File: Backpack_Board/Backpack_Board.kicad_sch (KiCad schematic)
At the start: 8 parts, among them J1 Conn_01x05, U7 MAX30102EFD_T

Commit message: Completed Backpack Board
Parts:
- removed J1: Conn_01x05, Connector_PinHeader_1.27mm:PinHeader_1x05_P1.27mm_Vertical, symbol Connector_Generic:Conn_01x05
- added J1, J2: Conn_01x03, Connector_PinHeader_1.27mm:PinHeader_1x03_P1.27mm_Vertical, symbol Connector_Generic:Conn_01x03
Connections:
- net +1V8: now also J2.3 (Pin_3)
- net GND: now also J2.1 (Pin_1)
- net MAX_INT: now also J2.2 (Pin_2)
- net SCL: now also J1.1 (Pin_1)
- net SDA: now also J1.2 (Pin_2)
- no-connect marks 1 -> 2
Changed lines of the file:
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@@
+	)
+	(no_connect
+		(at 54.61 101.6)
 	)
 	(no_connect
@@
 	(wire
 		(pts
+			(xy 63.5 82.55) (xy 54.61 82.55)
+		)
+		(stroke
+			(width 0)
+			(type default)
+		)
+	)
+	(wire
+		(pts
 			(xy 96.52 77.47) (xy 96.52 78.74)
 		)
@@
 	(wire
 		(pts
-			(xy 63.5 91.44) (xy 54.61 91.44)
-		)
-		(stroke
-			(width 0)
-			(type default)
-		)
-	)
-	(wire
-		(pts
 			(xy 115.57 119.38) (xy 115.57 120.65)
 		)
@@
 	(wire
 		(pts
+			(xy 54.61 80.01) (xy 63.5 80.01)
+		)
+		(stroke
+			(width 0)
+			(type default)
+		)
+	)
+	(wire
+		(pts
 			(xy 107.95 118.11) (xy 107.95 119.38)
 		)
@@
 	(wire
 		(pts
-			(xy 63.5 101.6) (xy 54.61 101.6)
-		)
-		(stroke
-			(width 0)
-			(type default)
-		)
-	)
-	(wire
-		(pts
 			(xy 139.7 109.22) (xy 139.7 106.68)
 		)
@@
 	(wire
 		(pts
-			(xy 63.5 93.98) (xy 54.61 93.98)
-		)
-		(stroke
-			(width 0)
-			(type default)
-		)
-	)
-	(wire
-		(pts
 			(xy 107.95 129.54) (xy 115.57 129.54)
 		)
@@
 	(wire
 		(pts
+			(xy 54.61 77.47) (xy 63.5 77.47)
+		)
+		(stroke
+			(width 0)
+			(type default)
+		)
+	)
+	(wire
+		(pts
 			(xy 115.57 128.27) (xy 115.57 129.54)
 		)
@@
 		)
 	)
-	(label "MAX_INT"
-		(at 63.5 93.98 180)
+	(label "+1V8"
+		(at 63.5 82.55 180)
 		(effects
 			(font
@@
 		)
 	)
-	(label "+1V8"
-		(at 63.5 91.44 180)
+	(label "GND"
+		(at 63.5 77.47 180)
 		(effects
 			(font
@@
 		)
 	)
-	(label "GND"
-		(at 63.5 101.6 180)
+	(label "MAX_INT"
+		(at 63.5 80.01 180)
 		(effects
 			(font
@@
 			)
 			(justify left bottom)
+		)
+	)
+	(symbol
+		(lib_id "Connector_Generic:Conn_01x03")
+		(at 49.53 80.01 0)
+		(mirror y)
+		(unit 1)
+		(body_style 1)
+		(exclude_from_sim no)
+		(in_bom yes)
+		(on_board yes)
+		(in_pos_files yes)
+		(dnp no)
+		(property "Reference" "J2"
+			(at 49.53 87.9645 0)
+			(show_name no)
+			(do_not_autoplace no)
+			(effects
+				(font
+					(size 1.27 1.27)
+				)
+			)
+		)
+		(property "Value" "Conn_01x03"
+			(at 49.53 85.5402 0)
+			(show_name no)
+			(do_not_autoplace no)
+			(effects
+				(font
+					(size 1.27 1.27)
+				)
+			)
+		)
+		(property "Footprint" "Connector_PinHeader_1.27mm:PinHeader_1x03_P1.27mm_Vertical"
+			(at 49.53 80.01 0)
+			(hide yes)
+			(show_name no)
+			(do_not_autoplace no)
+			(effects
+				(font
+					(size 1.27 1.27)
+				)
+			)
+		)
+		(property "Datasheet" ""
+			(at 49.53 80.01 0)
+			(hide yes)
+			(show_name no)
+			(do_not_autoplace no)
+			(effects
+				(font
+					(size 1.27 1.27)
+				)
+			)
+		)
+		(property "Description" "Generic connector, single row, 01x03, script generated (kicad-library-utils/schlib/autogen/connector/)"
+			(at 49.53 80.01 0)
+			(hide yes)
+			(show_name no)
+			(do_not_autoplace no)
+			(effects
+				(font
+					(size 1.27 1.27)
+				)
+			)
+		)
+		(pin "2"
+		)
+		(pin "1"
+		)
+		(pin "3"
+		)
+		(instances
+			(project "Backpack_Board"
+				(path "/49f0e556-777a-4724-8c92-dc192098b240"
+					(reference "J2")
+					(unit 1)
+				)
+			)
+		)
+	)
+	(symbol
+		(lib_id "Connector_Generic:Conn_01x03")
+		(at 49.53 99.06 0)
+		(mirror y)
+		(unit 1)
+		(body_style 1)
+		(exclude_from_sim no)
+		(in_bom yes)
+		(on_board yes)
+		(in_pos_files yes)
+		(dnp no)
+		(property "Reference" "J1"
+			(at 49.53 107.0145 0)
+			(show_name no)
+			(do_not_autoplace no)
+			(effects
+				(font
+					(size 1.27 1.27)
+				)
+			)
+		)
+		(property "Value" "Conn_01x03"
+			(at 49.53 104.5902 0)
+			(show_name no)
+			(do_not_autoplace no)
+			(effects
+				(font
+					(size 1.27 1.27)
+				)
+			)
+		)
+		(property "Footprint" "Connector_PinHeader_1.27mm:PinHeader_1x03_P1.27mm_Vertical"
+			(at 49.53 99.06 0)
+			(hide yes)
+			(show_name no)
+			(do_not_autoplace no)
+			(effects
+				(font
+					(size 1.27 1.27)
+				)
+			)
+		)
+		(property "Datasheet" ""
+			(at 49.53 99.06 0)
+			(hide yes)
+			(show_name no)
+			(do_not_autoplace no)
+			(effects
+				(font
+					(size 1.27 1.27)
+				)
+			)
+		)
+		(property "Description" "Generic connector, single row, 01x03, script generated (kicad-library-utils/schlib/autogen/connector/)"
+			(at 49.53 99.06 0)
+			(hide yes)
+			(show_name no)
+			(do_not_autoplace no)
+			(effects
+				(font
+					(size 1.27 1.27)
+				)
+			)
+		)
+		(pin "2"
+		)
+		(pin "1"
+		)
+		(pin "3"
+		)
+		(instances
+			(project "Backpack_Board"
+				(path "/49f0e556-777a-4724-8c92-dc192098b240"
+					(reference "J1")
+					(unit 1)
+				)
+			)
 		)
 	)
@@
 				)
 			)
-		)
-	)
-	(symbol
-		(lib_id "Connector_Generic:Conn_01x05")
-		(at 49.53 96.52 180)
-		(unit 1)
-		(body_style 1)
-		(exclude_from_sim no)
-		(in_bom yes)
-		(on_board yes)
-		(in_pos_files yes)
-		(dnp no)
-		(fields_autoplaced yes)
-		(property "Reference" "J1"
-			(at 49.53 86.0255 0)
-			(show_name no)
-			(do_not_autoplace no)
-			(effects
-				(font
-					(size 1.27 1.27)
-				)
-			)
-		)
-		(property "Value" "Conn_01x05"
-			(at 49.53 88.4498 0)
-			(show_name no)
-			(do_not_autoplace no)
-			(effects
-				(font
-					(size 1.27 1.27)
-				)
-			)
-		)
-		(property "Footprint" "Connector_PinHeader_1.27mm:PinHeader_1x05_P1.27mm_Vertical"
-			(at 49.53 96.52 0)
-			(hide yes)
-			(show_name no)
-			(do_not_autoplace no)
-			(effects
-				(font
-					(size 1.27 1.27)
-				)
-			)
-		)
-		(property "Datasheet" ""
-			(at 49.53 96.52 0)
-			(hide yes)
-			(show_name no)
-			(do_not_autoplace no)
-			(effects
-				(font
-					(size 1.27 1.27)
-				)
-			)
-		)
-		(property "Description" "Generic connector, single row, 01x05, script generated (kicad-library-utils/schlib/autogen/connector/)"
-			(at 49.53 96.52 0)
-			(hide yes)
-			(show_name no)
-			(do_not_autoplace no)
-			(effects
-				(font
-					(size 1.27 1.27)
-				)
-			)
-		)
-		(pin "2"
-		)
-		(pin "1"
-		)
-		(pin "3"
-		)
-		(pin "4"
-		)
-		(pin "5"
-		)
-		(instances
-			(project "Backpack_Board"
-				(path "/49f0e556-777a-4724-8c92-dc192098b240"
-					(reference "J1")
-					(unit 1)
-				)
-			)

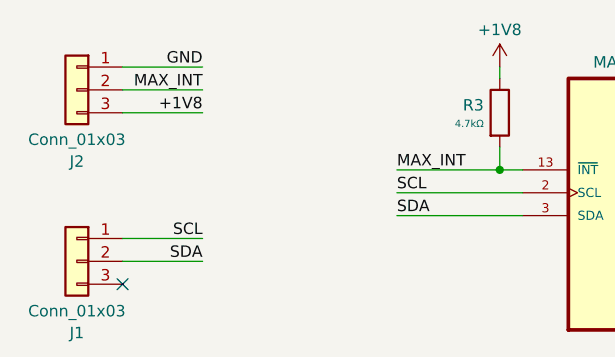
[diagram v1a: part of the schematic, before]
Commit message: Layout Midpoint, Updated Backpack Schem
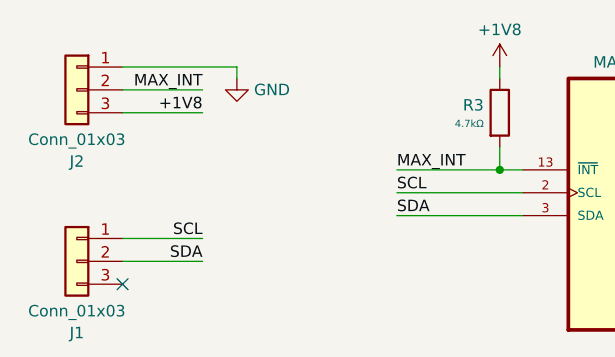
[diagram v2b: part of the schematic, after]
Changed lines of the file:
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@@
+	(wire
+		(pts
+			(xy 67.31 77.47) (xy 67.31 78.74)
+		)
+		(stroke
+			(width 0)
+			(type default)
+		)
+	)
 	(wire
 		(pts
@@
 	(wire
 		(pts
-			(xy 54.61 77.47) (xy 63.5 77.47)
+			(xy 54.61 77.47) (xy 67.31 77.47)
 		)
 		(stroke
@@
 			)
 			(justify left bottom)
-		)
-	)
-	(label "GND"
-		(at 63.5 77.47 180)
-		(effects
-			(font
-				(size 1.27 1.27)
-			)
-			(justify right bottom)
 		)
 	)
@@
 					(unit 1)
 				)
+			)
+		)
+	)
+	(symbol
+		(lib_id "power:GND")
+		(at 67.31 78.74 0)
+		(unit 1)
+		(body_style 1)
+		(exclude_from_sim no)
+		(in_bom yes)
+		(on_board yes)
+		(in_pos_files yes)
+		(dnp no)
+		(fields_autoplaced yes)
+		(property "Reference" "#PWR08"
+			(at 67.31 85.09 0)
+			(hide yes)
+			(show_name no)
+			(do_not_autoplace no)
+			(effects
+				(font
+					(size 1.27 1.27)
+				)
+			)
+		)
+		(property "Value" "GND"
+			(at 69.215 80.01 0)
+			(show_name no)
+			(do_not_autoplace no)
+			(effects
+				(font
+					(size 1.27 1.27)
+				)
+				(justify left)
+			)
+		)
+		(property "Footprint" ""
+			(at 67.31 78.74 0)
+			(hide yes)
+			(show_name no)
+			(do_not_autoplace no)
+			(effects
+				(font
+					(size 1.27 1.27)
+				)
+			)
+		)
+		(property "Datasheet" ""
+			(at 67.31 78.74 0)
+			(hide yes)
+			(show_name no)
+			(do_not_autoplace no)
+			(effects
+				(font
+					(size 1.27 1.27)
+				)
+			)
+		)
+		(property "Description" "Power symbol creates a global label with name \"GND\" , ground"
+			(at 67.31 78.74 0)
+			(hide yes)
+			(show_name no)
+			(do_not_autoplace no)
+			(effects
+				(font
+					(size 1.27 1.27)
+				)
+			)
+		)
+		(pin "1"
+		)
+		(instances
+			(project "Backpack_Board"
+				(path "/49f0e556-777a-4724-8c92-dc192098b240"
+					(reference "#PWR08")
+					(unit 1)
+				)

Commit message: Updated Keepout and Started Case Model
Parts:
- C1: Price 0.009USD -> (none)
- C2, C4: Price 0.006USD -> (none)
- C3: Price 0.013USD -> (none)
- J1, J2: now left out of the parts list
- R3: Price 0.004USD -> (none)
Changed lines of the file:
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@@
 		(body_style 1)
 		(exclude_from_sim no)
-		(in_bom yes)
+		(in_bom no)
 		(on_board yes)
 		(in_pos_files yes)
@@
 		(body_style 1)
 		(exclude_from_sim no)
-		(in_bom yes)
+		(in_bom no)
 		(on_board yes)
 		(in_pos_files yes)
@@
 			)
 		)
-		(property "Price" "0.006USD"
-			(at 115.57 124.46 0)
-			(hide yes)
-			(show_name no)
-			(do_not_autoplace no)
-			(effects
-				(font
-					(size 1.27 1.27)
-				)
-			)
-		)
 		(property "Process" "SMT"
 			(at 115.57 124.46 0)
@@
 			)
 		)
-		(property "Price" "0.009USD"
-			(at 88.9 124.46 0)
-			(hide yes)
-			(show_name no)
-			(do_not_autoplace no)
-			(effects
-				(font
-					(size 1.27 1.27)
-				)
-			)
-		)
 		(property "Process" "SMT"
 			(at 88.9 124.46 0)
@@
 		)
 		(property "Stock" "4246728"
-			(at 107.95 124.46 0)
-			(hide yes)
-			(show_name no)
-			(do_not_autoplace no)
-			(effects
-				(font
-					(size 1.27 1.27)
-				)
-			)
-		)
-		(property "Price" "0.013USD"
 			(at 107.95 124.46 0)
 			(hide yes)
@@
 			)
 		)
-		(property "Price" "0.004USD"
-			(at 96.52 82.55 0)
-			(hide yes)
-			(show_name no)
-			(do_not_autoplace no)
-			(effects
-				(font
-					(size 1.27 1.27)
-				)
-			)
-		)
 		(property "Process" "SMT"
 			(at 96.52 82.55 0)
@@
 			(at 96.52 124.46 0)
 			(hide yes)
-			(show_name no)
-			(do_not_autoplace no)
-			(effects
-				(font
-					(size 1.27 1.27)
-				)
-			)
-		)
-		(property "Price" "0.006USD"
-			(at 96.52 124.46 0)
-			(hide yes)
